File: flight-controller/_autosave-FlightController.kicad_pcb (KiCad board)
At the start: 2 copper layers, 57 x 37 mm, 37 parts, among them J1 MSD-4-A, J2 Conn_01x03_Pin, J3 Conn_01x03_Pin, J4 Conn_01x03_Pin, J5 Conn_01x03_Pin, J6 USB4215-03-A_REVA, J7 Conn_01x03_Pin, J8 Conn_01x03_Pin, J9 Conn_01x04_Pin, U1 ESP32-S3-WROOM-1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

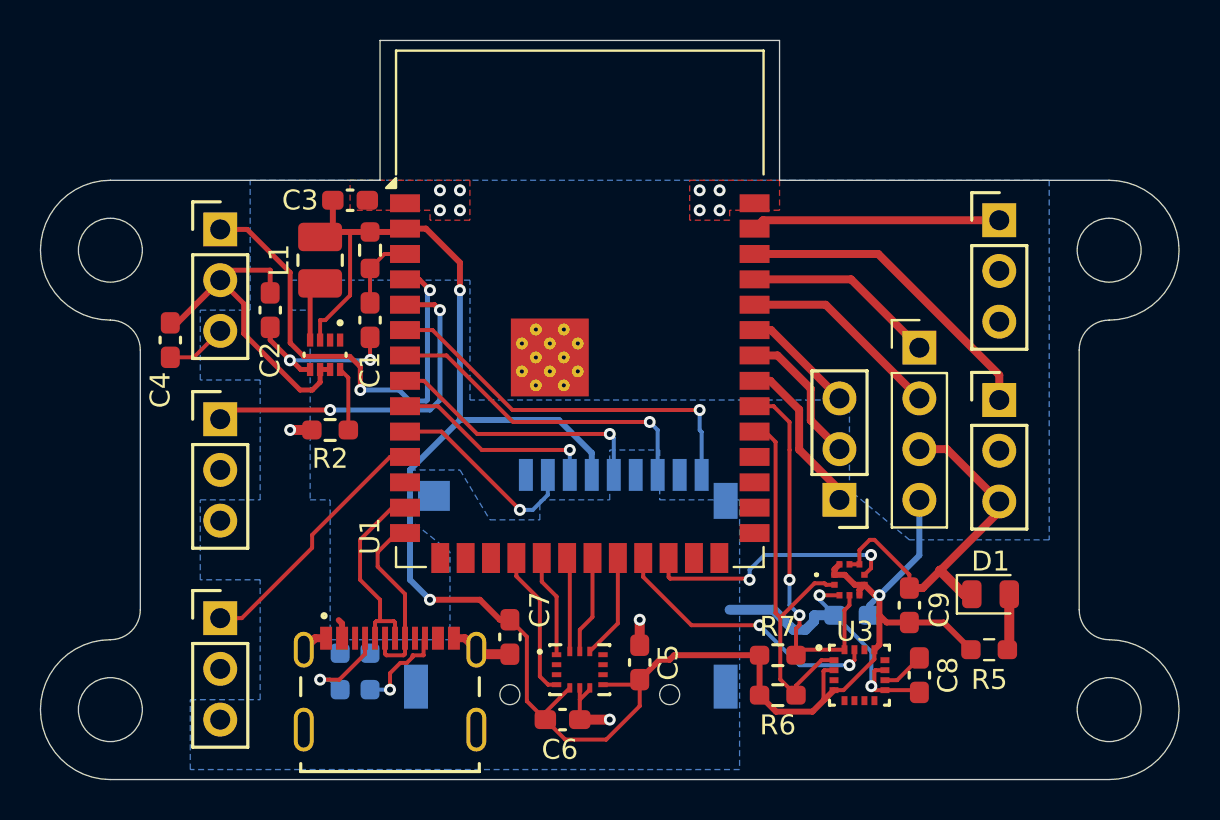
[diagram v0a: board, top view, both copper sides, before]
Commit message: esd protection
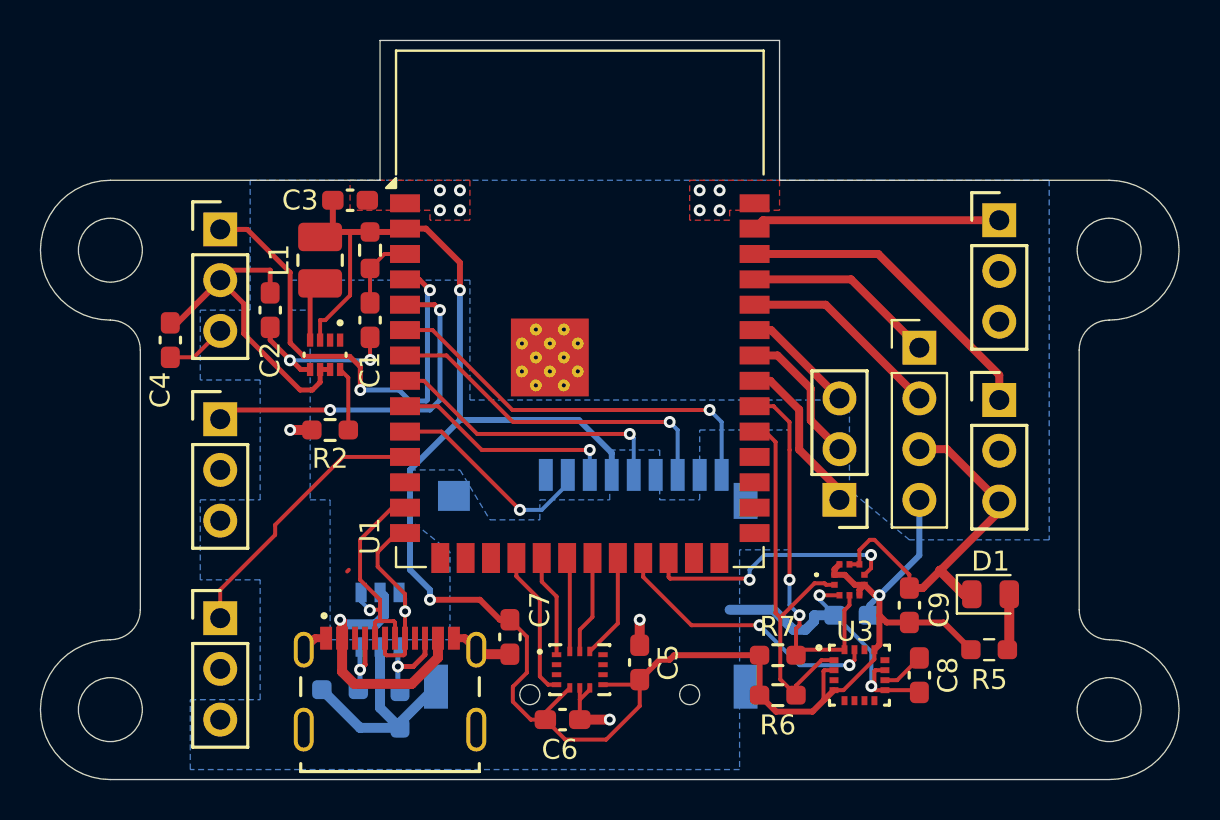
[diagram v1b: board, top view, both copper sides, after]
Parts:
- added CR1: USBLC6-4SC6, footprints:SOT23-6L_STM, B.Cu at (100.0, 72.0)
- moved R3 2.43 mm to (101.0, 76.5), turned to 90 degrees
- moved J1 1.00 mm to (110.5, 72.5)
- moved R4 0.91 mm to (98.0, 75.5), turned to 0 degrees
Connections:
- net Net-(J6-CC1) renamed CC1
- net Net-(J6-CC2) renamed CC2
- J6 pad A4_B9: +5V -> 5V_USB
- J6 pad B4_A9: +5V -> 5V_USB
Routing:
- net 5V_USB: track 0.00 -> 13.1 mm, vias 0 -> 1
- net GND: track 58.5 -> 70.2 mm
- net +3.3V: track 99.9 -> 101.9 mm
- net SD_MISO: track 16.5 -> 18.3 mm
- net DATA-: track 10.0 -> 11.7 mm, vias 0 -> 1
- net DATA+: track 9.27 -> 10.4 mm, vias 0 -> 1
- net SD_MOSI: track 10.4 -> 11.4 mm
- net SD_CLK: track 13.5 -> 14.5 mm
- net +5V: track 17.7 -> 16.7 mm
- net CC1: track 4.78 -> 3.87 mm
- net RECEIVER: track 13.0 -> 13.7 mm
- net SD_CD: track 19.7 -> 20.4 mm
- net SD_CS: track 10.1 -> 10.8 mm
